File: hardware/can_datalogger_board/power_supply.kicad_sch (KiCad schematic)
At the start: 17 parts, among them U6 R-78B5.0-2.0, U7 TLE42744DV33ATMA1

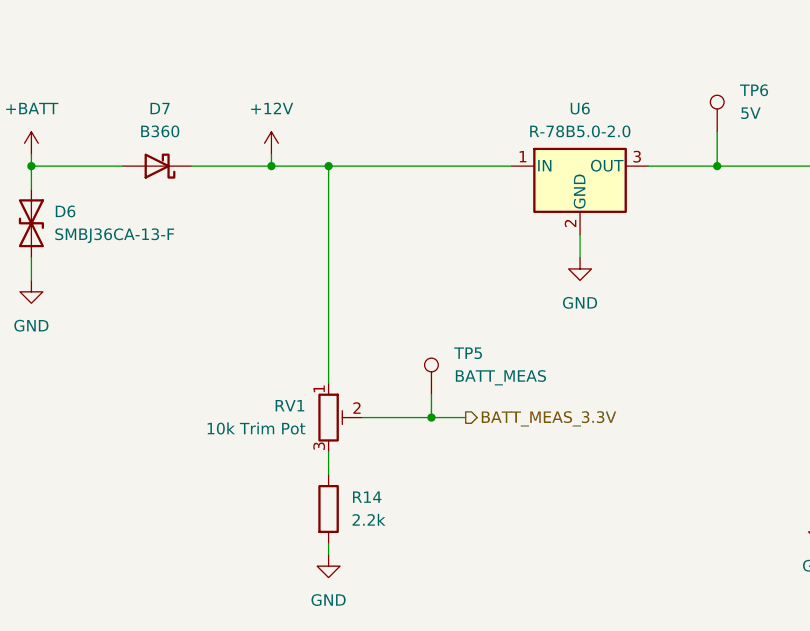
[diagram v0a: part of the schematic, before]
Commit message: PCB component placement
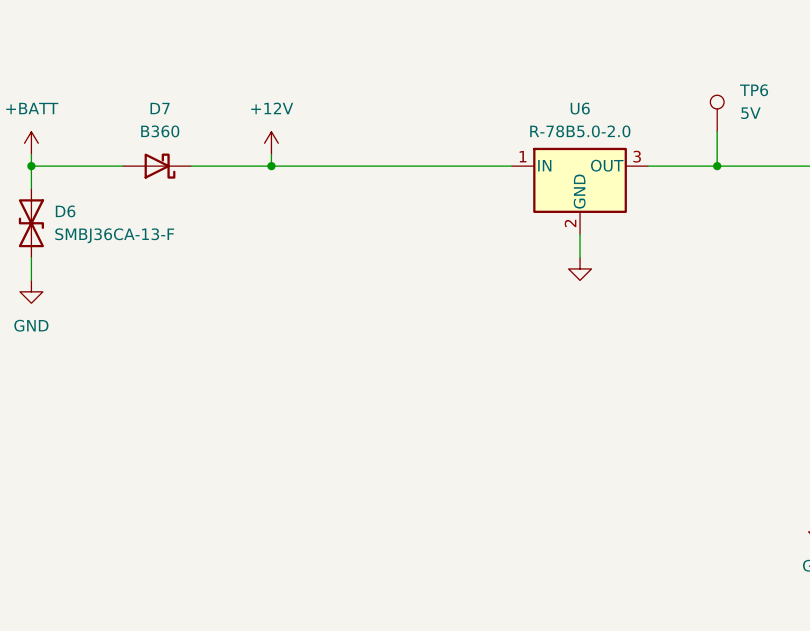
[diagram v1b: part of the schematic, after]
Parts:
- removed R14: 2.2k, Resistor_SMD:R_0603_1608Metric, symbol Device:R
- removed RV1: 10k Trim Pot, Potentiometer_SMD:Potentiometer_Bourns_TC33X_Vertical, symbol Device:R_Potentiometer_Trim
- removed TP5: BATT_MEAS, TestPoint:TestPoint_Pad_D1.0mm, symbol Connector:TestPoint
